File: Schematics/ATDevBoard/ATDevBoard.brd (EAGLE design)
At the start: 67.7 x 54.4 mm, 40 parts, among them U1 TINY85-DIP

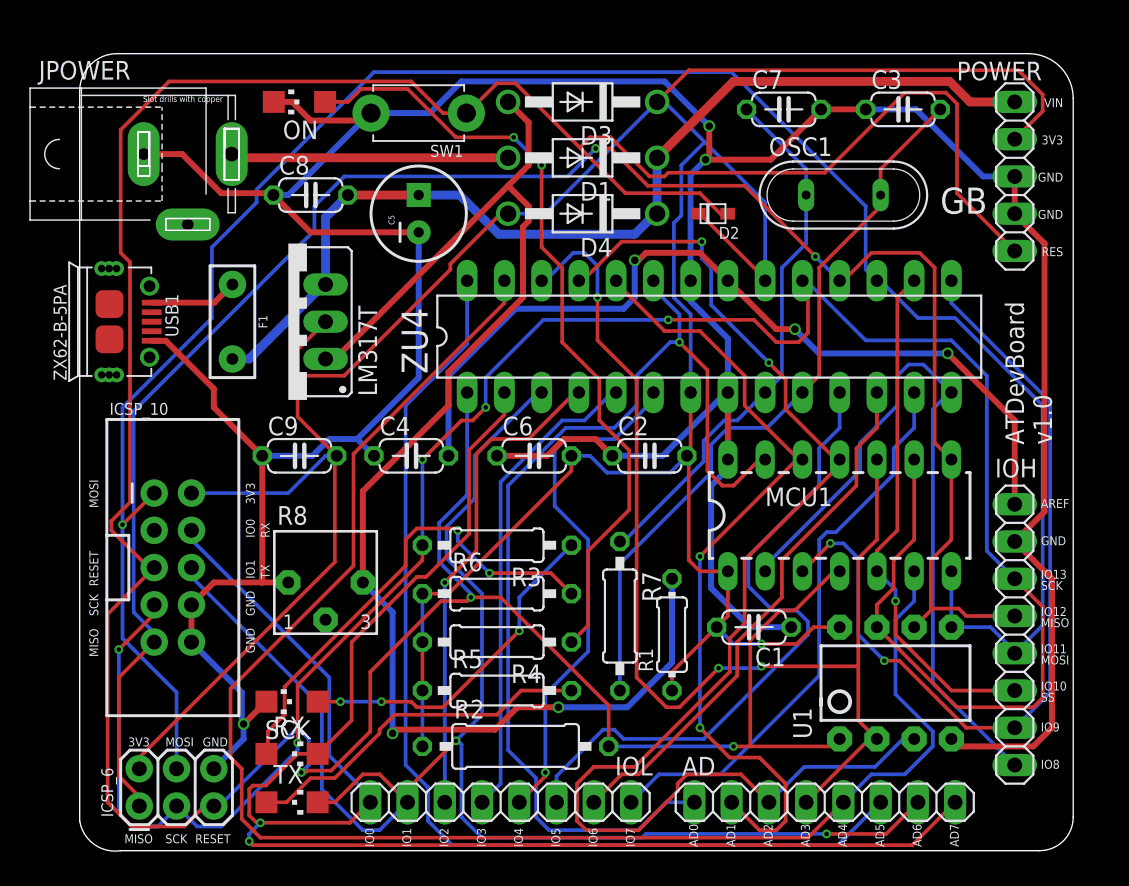
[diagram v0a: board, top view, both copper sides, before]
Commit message: Removed diode for reset line, revisted layout for oscillator
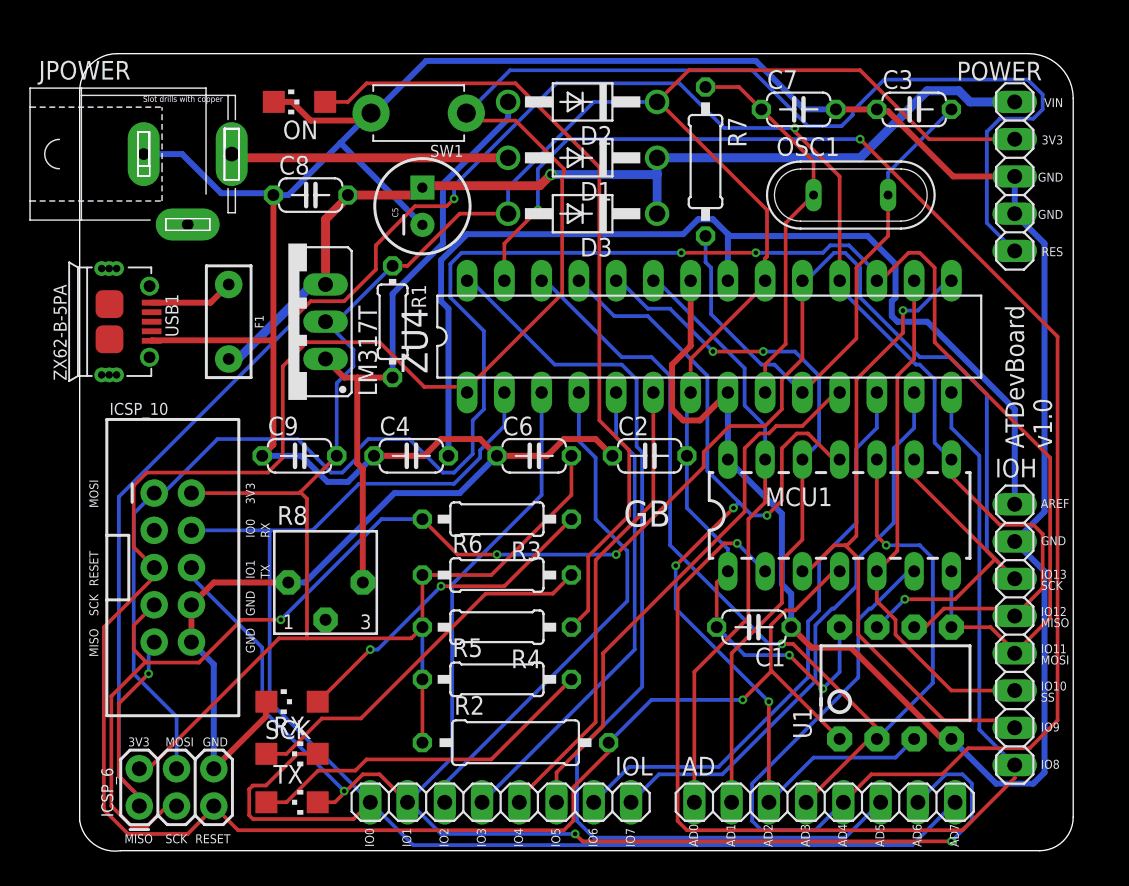
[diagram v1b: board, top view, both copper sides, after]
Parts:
- removed D4: 1N4007, diode:DO41-10
- D2: value 1N4148 -> 1N4007; device adafruit:SOD-323F -> diode:DO41-10
- moved R7 31.5 mm to (42.4, 46.5)
- moved R1 28.6 mm to (21.1, 35.6), turned to 270 degrees
- moved D2 11.7 mm to (34.0, 50.5)
- moved D3 7.62 mm to (34.0, 42.9)
- moved R3 1.78 mm to (28.2, 22.1)
- moved R6 1.27 mm to (28.2, 18.3)
- moved R4 1.02 mm to (28.2, 14.7)
- moved C7 1.02 mm to (48.8, 50.0)
- moved C3 0.76 mm to (56.6, 50.0)
- moved R5 0.76 mm to (28.2, 11.2)
- moved C5 0.57 mm to (23.1, 43.4)
- moved OSC1 0.51 mm to (52.3, 44.2)
- moved F1 0.25 mm to (9.91, 35.6)
- moved R2 0.25 mm to (29.5, 6.86)
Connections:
- net +3V3: now also D3.A; no longer D3.C, D4.A
- net N$1: now also D2.A; no longer D3.A
- net RESET: no longer D2.A
- net VIN: now also D3.C; no longer D4.C
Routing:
- net N$1: track 94.4 -> 41.3 mm, vias 2 -> 0
- net AD0: track 71.8 -> 40.9 mm, vias 1 -> 0
- net RESET: track 239.9 -> 210.6 mm, vias 3 -> 1
- net +3V3: track 221.3 -> 194.6 mm, vias 1 -> 2
- net IO8: track 50.2 -> 76.6 mm, vias 0 -> 1
- net AD2: track 89.9 -> 69.9 mm, vias 2 -> 4
- net SCK: track 155.7 -> 136.6 mm, vias 5 -> 4
- net MISO: track 129.0 -> 145.3 mm, vias 2 -> 4
- net GND: track 261.0 -> 276.6 mm, vias 3 -> 0
- net IO0: track 121.4 -> 106.8 mm, vias 2 -> 0
- net AD4: track 108.5 -> 122.7 mm, vias 0 -> 2
- net XTAL2: track 50.2 -> 37.4 mm
- net IO9: track 57.8 -> 45.2 mm, vias 2 -> 1
- net AREF: track 59.5 -> 71.3 mm, vias 3 -> 0
- net XTAL1: track 37.1 -> 26.6 mm
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
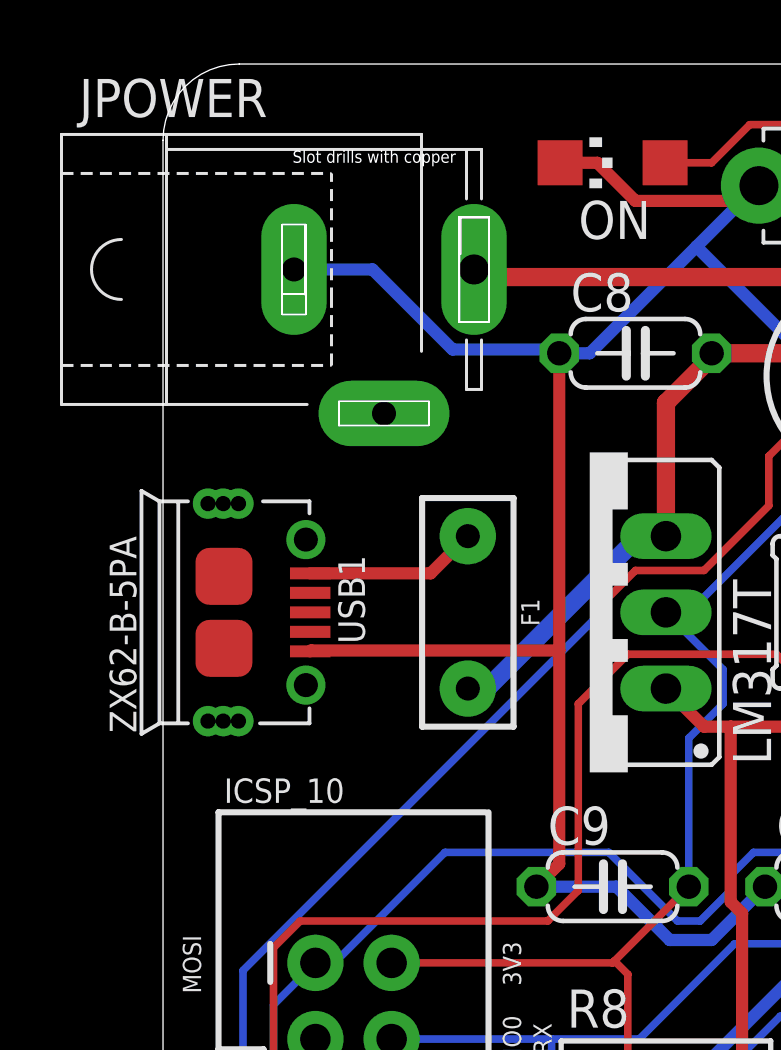
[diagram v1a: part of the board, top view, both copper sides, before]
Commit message: Replaced USB micro connector with Molex one
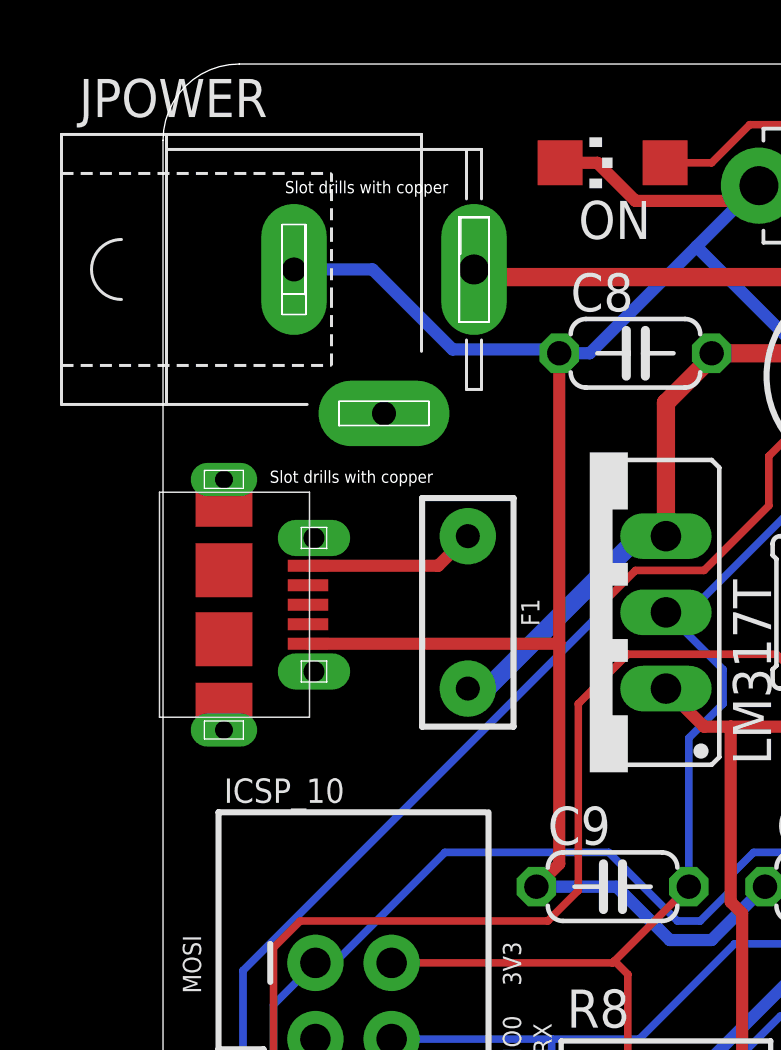
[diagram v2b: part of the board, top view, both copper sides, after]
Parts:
- R8: value (none) -> 2K
- USB1: value ZX62-B-5PA -> MOLEX47589; device Seeed-Connector:MICRO-USB5+6P-SMD-0.65-AB -> con-molex-usb:47589-0001
- moved USB1 0.25 mm to (1.78, 35.8), turned to 0 degrees
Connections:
- net VBUS renamed VUSB
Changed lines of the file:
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@@
 v1.0</text>
 <text x="36.83" y="21.59" size="1.778" layer="25">GB</text>
-<text x="4.064" y="50.546" size="0.4064" layer="46">Slot drills with copper</text>
+<text x="3.81" y="49.53" size="0.4064" layer="46">Slot drills with copper</text>
 <text x="2.794" y="0" size="0.6096" layer="25">MISO</text>
 <text x="5.588" y="0" size="0.6096" layer="25">SCK</text>
@@
 <text x="12.7" y="20.828" size="0.6096" layer="25" rot="R90">RX</text>
 <text x="12.7" y="18.034" size="0.6096" layer="25" rot="R90">TX</text>
+<text x="3.302" y="39.878" size="0.4064" layer="46">Slot drills with copper</text>
 </plain>
 <attributes>
@@
 </class>
 <class number="2" name="gnd" width="0.4064" drill="0.508">
-<clearance class="2" value="0.254"/>
+<clearance class="2" value="0.127"/>
 </class>
 <class number="3" name="aref" width="0.4064" drill="0.508">
@@
 <attribute name="PROD_ID" value="RES-08490" x="9.906" y="35.56" size="1.778" layer="27" rot="R270" display="off"/>
 </element>
-<element name="USB1" library="Seeed-Connector" package="MICRO-USB5+6P-SMD-0.65-AB" value="ZX62-B-5PA" x="1.778" y="35.56" rot="R270">
-<attribute name="MPN" value="ZX62-B-5PA" x="1.778" y="35.56" size="1.778" layer="27" rot="R270" display="off"/>
-</element>
-<element name="R8" library="bourns" package="3362R" value="" x="16.51" y="17.78"/>
+<element name="R8" library="bourns" package="3362R" value="2K" x="16.51" y="17.78"/>
+<element name="USB1" library="con-molex-usb" package="47589-0001" value="MOLEX47589" x="1.778" y="35.814"/>
 </elements>
 <signals>
@@
 <contactref element="ON" pad="C"/>
 <contactref element="JPOWER" pad="1"/>
-<contactref element="USB1" pad="5"/>
 <contactref element="POWER" pad="2"/>
 <contactref element="POWER" pad="3"/>
@@
 <wire x1="25.654" y1="23.876" x2="21.209" y2="23.876" width="0.4064" layer="16"/>
 <wire x1="28.194" y1="26.416" x2="25.654" y2="23.876" width="0.4064" layer="16"/>
-<wire x1="12.954" y1="27.178" x2="12.954" y2="34.29" width="0.4064" layer="1"/>
-<wire x1="12.954" y1="34.29" x2="12.954" y2="44.196" width="0.4064" layer="1"/>
+<wire x1="12.954" y1="27.178" x2="12.954" y2="34.544" width="0.4064" layer="1"/>
+<wire x1="12.954" y1="34.544" x2="12.954" y2="44.196" width="0.4064" layer="1"/>
 <wire x1="12.192" y1="26.416" x2="12.954" y2="27.178" width="0.4064" layer="1"/>
 <wire x1="49.149" y1="50.038" x2="51.308" y2="50.038" width="0.4064" layer="16"/>
@@
 <wire x1="19.812" y1="49.784" x2="23.368" y2="53.34" width="0.4064" layer="16"/>
 <wire x1="19.812" y1="49.784" x2="19.61" y2="49.784" width="0.4064" layer="16"/>
-<wire x1="4.653" y1="34.26" x2="4.683" y2="34.29" width="0.4064" layer="1"/>
-<wire x1="4.683" y1="34.29" x2="12.954" y2="34.29" width="0.4064" layer="1"/>
+<contactref element="USB1" pad="5"/>
+<wire x1="4.578" y1="34.514" x2="12.924" y2="34.514" width="0.4064" layer="1"/>
+<wire x1="12.924" y1="34.514" x2="12.954" y2="34.544" width="0.4064" layer="1"/>
 </signal>
 <signal name="AREF" class="3">
@@
 <wire x1="10.16" y1="46.99" x2="10.112" y2="46.99" width="0.6096" layer="1"/>
 </signal>
-<signal name="VBUS" class="4">
+<signal name="VUSB">
 <contactref element="F1" pad="P$1"/>
 <contactref element="USB1" pad="1"/>
-<wire x1="4.653" y1="36.86" x2="8.666" y2="36.86" width="0.4064" layer="1"/>
-<wire x1="8.666" y1="36.86" x2="9.906" y2="38.1" width="0.4064" layer="1"/>
+<wire x1="4.578" y1="37.114" x2="8.92" y2="37.114" width="0.4064" layer="1"/>
+<wire x1="8.92" y1="37.114" x2="9.906" y2="38.1" width="0.4064" layer="1"/>
 </signal>
 </signals>

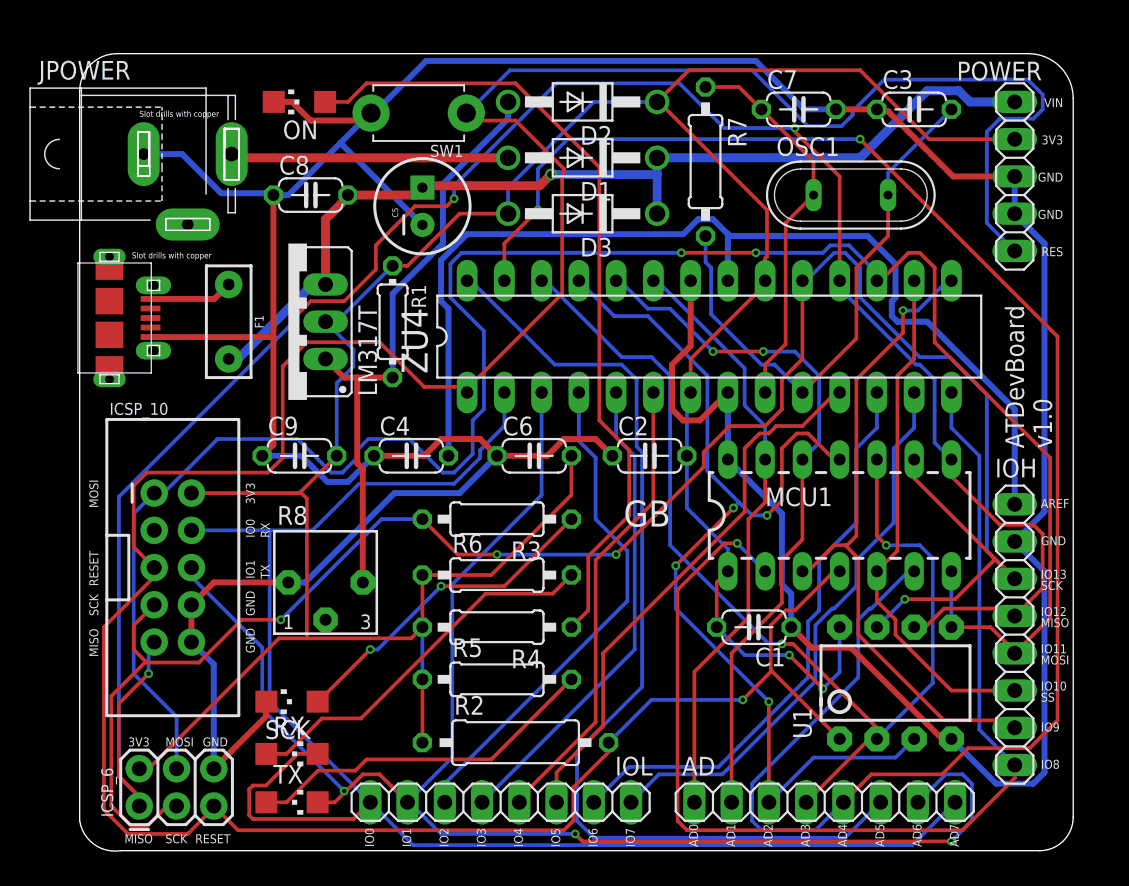
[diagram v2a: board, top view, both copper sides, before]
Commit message: Fidex schematic for trimmer, added jumper for VCC, schematic tested on breadboard
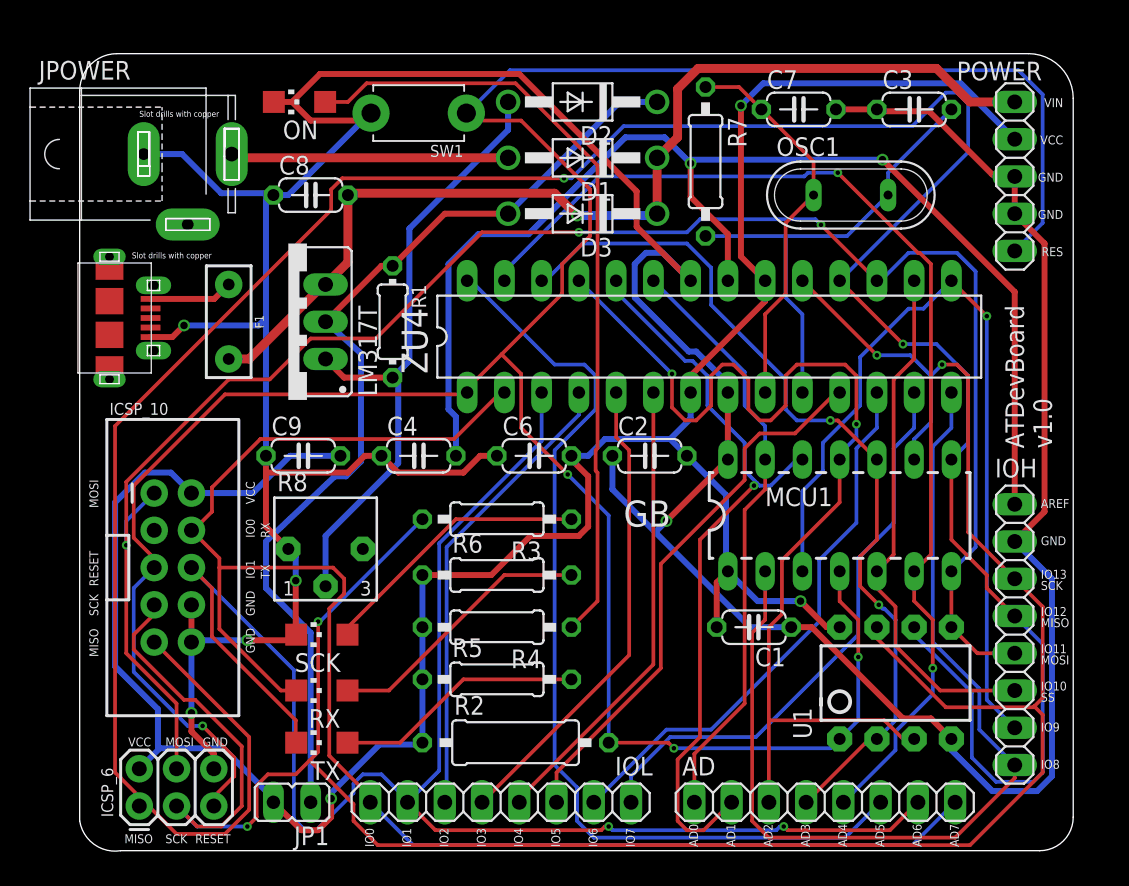
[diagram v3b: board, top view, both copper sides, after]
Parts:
- removed C5: 100uf, SparkFun-Capacitors:CPOL-RADIAL-100UF-25V
- added JP1: (no value), jumper:JP1
- ON: value GREEN -> RED
- moved SCK 5.00 mm to (16.3, 14.2)
- moved RX 4.77 mm to (16.3, 10.4), turned to 90 degrees
- moved TX 4.54 mm to (16.3, 6.86), turned to 90 degrees
- moved R8 2.29 mm to (16.5, 20.1)
- moved C4 0.51 mm to (22.9, 26.4)
- moved C9 0.25 mm to (15.0, 26.4)
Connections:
- removed net +3V3: C1.2, C2.2, C6.2, C9.2, D2.C, D3.A, ICSP_10.2, ICSP_6.2, LM317T.2, MCU1.1, POWER.4, R1.1, R2.1, R4.2, R5.1, R6.1, U1.8, ZU4.20, ZU4.7
- new net N$5: D2.C, D3.A, JP1.1, LM317T.2, R1.1
- new net VCC: C1.2, C2.2, C6.2, C9.2, ICSP_10.2, ICSP_6.2, JP1.2, MCU1.1, POWER.4, R2.1, R4.2, R5.1, R6.1, U1.8, ZU4.20, ZU4.7
- net GND: no longer C5.2
- net N$1: now also R8.2; no longer R8.3
- net VIN: no longer C5.1
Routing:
- net +3V3: track 194.6 -> 0.00 mm, vias 2 -> 0
- net VCC: track 0.00 -> 169.3 mm, vias 0 -> 3
- net N$5: track 0.00 -> 67.1 mm
- net AD4: track 122.7 -> 75.3 mm
- net MISO: track 145.3 -> 191.9 mm, vias 4 -> 2
- net SCK: track 136.6 -> 174.9 mm
- net RESET: track 210.6 -> 191.1 mm, vias 1 -> 4
- net MOSI: track 137.2 -> 123.7 mm, vias 2 -> 3
- net AD3: track 73.2 -> 60.4 mm
- net AREF: track 71.3 -> 83.7 mm, vias 0 -> 2
- net IO9: track 45.2 -> 56.9 mm
- net GND: track 276.7 -> 265.2 mm, vias 0 -> 5
- net IO8: track 76.6 -> 66.6 mm, vias 1 -> 0
- net IO1: track 106.5 -> 114.4 mm, vias 3 -> 2
- net N$35: track 25.9 -> 18.5 mm
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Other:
- board text added: "VCC"
- board text removed: "3V3"
